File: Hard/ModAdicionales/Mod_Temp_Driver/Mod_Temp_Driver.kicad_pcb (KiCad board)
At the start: 2 copper layers, 70 x 100 mm, 0 parts

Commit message: Inicio placement de componentes en Modulos Adicionales
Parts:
- added C301: 1nF, Capacitor_SMD:C_0805_2012Metric_Pad1.15x1.40mm_HandSolder, F.Cu at (100.0, 137.0)
- added C302: 1nF, Capacitor_SMD:C_0805_2012Metric_Pad1.15x1.40mm_HandSolder, F.Cu at (107.5, 136.5)
- added C303: 1nF, Capacitor_SMD:C_0805_2012Metric_Pad1.15x1.40mm_HandSolder, F.Cu at (115.5, 138.0)
- added C304: 1nF, Capacitor_SMD:C_0805_2012Metric_Pad1.15x1.40mm_HandSolder, F.Cu at (104.0, 137.0)
- added C401: 100nF, Capacitor_SMD:C_0805_2012Metric_Pad1.15x1.40mm_HandSolder, F.Cu at (138.5, 135.0)
- added C402: 1nF, Capacitor_SMD:C_0805_2012Metric_Pad1.15x1.40mm_HandSolder, F.Cu at (138.5, 139.0)
- added C501: 2.2uf, Capacitor_THT:CP_Radial_D5.0mm_P2.00mm, F.Cu at (43.6, 76.8)
- added C502: 470nF x 400v, Capacitor_THT:C_Rect_L16.5mm_W8.7mm_P15.00mm_MKT, F.Cu at (4.65, 55.6)
- added D201: 1N4007, Diode_THT:D_DO-41_SOD81_P10.16mm_Horizontal, F.Cu at (81.0, 105.0)
- added D301: D_Zener 12v, Diode_THT:D_DO-35_SOD27_P7.62mm_Horizontal, F.Cu at (104.5, 125.0)
- added D401: 1N4148, Diode_THT:D_DO-35_SOD27_P7.62mm_Horizontal, F.Cu at (86.5, 130.5)
- added D402: 1N4148, Diode_THT:D_DO-35_SOD27_P7.62mm_Horizontal, F.Cu at (114.5, 117.0)
- added D403: 1N4148, Diode_THT:D_DO-35_SOD27_P7.62mm_Horizontal, F.Cu at (115.0, 102.5)
- added D501: 1N4148, Diode_THT:D_DO-35_SOD27_P7.62mm_Horizontal, F.Cu at (138.0, 72.5)
- added D502: 1N4007, Diode_THT:D_DO-41_SOD81_P10.16mm_Horizontal, F.Cu at (49.0, 50.6)
- added D503: 1N4148, Diode_SMD:D_MiniMELF, F.Cu at (90.0, 68.0)
- added H201: MountingHole, MountingHole:MountingHole_3.2mm_M3, F.Cu at (73.5, 52.5)
- added H202: MountingHole, MountingHole:MountingHole_3.2mm_M3, F.Cu at (73.5, 85.5)
- added H203: MountingHole, MountingHole:MountingHole_3.2mm_M3, F.Cu at (136.5, 52.5)
- added H204: MountingHole, MountingHole:MountingHole_3.2mm_M3, F.Cu at (136.5, 85.5)
- added H501: MountingHole, MountingHole:MountingHole_3.2mm_M3, F.Cu at (73.5, 92.5)
- added H502: MountingHole, MountingHole:MountingHole_3.2mm_M3, F.Cu at (73.5, 145.5)
- added H503: MountingHole, MountingHole:MountingHole_3.2mm_M3, F.Cu at (136.5, 92.5)
- added H504: MountingHole, MountingHole:MountingHole_3.2mm_M3, F.Cu at (136.5, 145.5)
- added J201: Conn_01x11_Female, Conectores:TerminalBlock_bornier-11_P5.00mm, F.Cu at (79.8, 93.0)
- added J202: Conn_02x05_Odd_Even, Connector_PinHeader_2.54mm:PinHeader_2x05_P2.54mm_Horizontal, F.Cu at (92.5, 142.5)
- added J203: Conn_02x10_Odd_Even, Connector_PinHeader_2.54mm:PinHeader_2x10_P2.54mm_Horizontal, F.Cu at (127.4, 142.5)
- added J501: Conn_02x10_Odd_Even, Connector_PinHeader_2.54mm:PinHeader_2x10_P2.54mm_Horizontal, F.Cu at (82.6, 55.5)
- added J502: Conn_02x05_Odd_Even, Connector_PinHeader_2.54mm:PinHeader_2x05_P2.54mm_Horizontal, F.Cu at (117.5, 55.5)
- added J503: Conn_01x06_Male, Conectores:TerminalBlock_bornier-6_P5.00mm, F.Cu at (117.5, 85.0)
- added K401: G5LE-1, Relay_THT:Relay_SPDT_Omron-G5LE-1, F.Cu at (92.0, 119.0)
- added K402: G5LE-1, Relay_THT:Relay_SPDT_Omron-G5LE-1, F.Cu at (119.5, 123.5)
- added K403: G5LE-1, Relay_THT:Relay_SPDT_Omron-G5LE-1, F.Cu at (119.5, 106.0)
- added K501: G5LE-1, Relay_THT:Relay_SPDT_Omron-G5LE-1, F.Cu at (132.5, 68.5)
- added Q401: BC857, Package_TO_SOT_SMD:SOT-23, F.Cu at (91.0, 131.5)
- added Q402: BC857, Package_TO_SOT_SMD:SOT-23, F.Cu at (125.5, 121.0)
- added Q403: BC857, Package_TO_SOT_SMD:SOT-23, F.Cu at (125.0, 103.5)
- added Q501: BC857, Package_TO_SOT_SMD:SOT-23, F.Cu at (99.0, 62.0)
- added R301: 220K, Resistor_SMD:R_0805_2012Metric_Pad1.15x1.40mm_HandSolder, F.Cu at (98.5, 125.0)
- added R302: 1ohm 1/4w, Resistor_THT:R_Axial_DIN0207_L6.3mm_D2.5mm_P7.62mm_Horizontal, F.Cu at (111.0, 111.0)
- added R303: 330K 1/4w (carbón), Resistor_THT:R_Axial_DIN0207_L6.3mm_D2.5mm_P7.62mm_Horizontal, F.Cu at (80.4, 109.0)
- added R304: 330K 1/4w (carbón), Resistor_THT:R_Axial_DIN0207_L6.3mm_D2.5mm_P7.62mm_Horizontal, F.Cu at (91.0, 109.0)
- added R305: 330K 1/4w (carbón), Resistor_THT:R_Axial_DIN0207_L6.3mm_D2.5mm_P7.62mm_Horizontal, F.Cu at (99.0, 112.0)
- added R306: 22K, Resistor_SMD:R_0805_2012Metric_Pad1.15x1.40mm_HandSolder, F.Cu at (98.5, 122.5)
- added R307: 1ohm 1/4w, Resistor_THT:R_Axial_DIN0207_L6.3mm_D2.5mm_P7.62mm_Horizontal, F.Cu at (111.0, 102.0)
- added R308: 1ohm 1/4w, Resistor_THT:R_Axial_DIN0207_L6.3mm_D2.5mm_P7.62mm_Horizontal, F.Cu at (111.0, 114.0)
- added R309: 1ohm 1/4w, Resistor_THT:R_Axial_DIN0207_L6.3mm_D2.5mm_P7.62mm_Horizontal, F.Cu at (111.0, 108.0)
- added R310: 220 1/4w, Resistor_THT:R_Axial_DIN0207_L6.3mm_D2.5mm_P7.62mm_Horizontal, F.Cu at (109.0, 125.0)
- added R311: 1ohm 1/4w, Resistor_THT:R_Axial_DIN0207_L6.3mm_D2.5mm_P7.62mm_Horizontal, F.Cu at (111.0, 105.0)
- added R312: 10k, Resistor_SMD:R_0805_2012Metric_Pad1.15x1.40mm_HandSolder, F.Cu at (97.5, 131.5)
- added R313: RA, Resistor_SMD:R_0805_2012Metric_Pad1.15x1.40mm_HandSolder, F.Cu at (109.5, 127.7)
- added R314: 1k, Resistor_SMD:R_0805_2012Metric_Pad1.15x1.40mm_HandSolder, F.Cu at (109.5, 129.5)
- added R315: 22k, Resistor_SMD:R_0805_2012Metric_Pad1.15x1.40mm_HandSolder, F.Cu at (113.5, 127.5)
- added R316: 150k, Resistor_SMD:R_0805_2012Metric_Pad1.15x1.40mm_HandSolder, F.Cu at (113.5, 129.5)
- added R317: 10k, Resistor_SMD:R_0805_2012Metric_Pad1.15x1.40mm_HandSolder, F.Cu at (115.5, 134.0)
- added R401: 10k, Resistor_SMD:R_0805_2012Metric_Pad1.15x1.40mm_HandSolder, F.Cu at (94.0, 129.5)
- added R402: 1M, Resistor_SMD:R_0805_2012Metric_Pad1.15x1.40mm_HandSolder, F.Cu at (91.0, 128.5)
- added R403: 10k, Resistor_SMD:R_0805_2012Metric_Pad1.15x1.40mm_HandSolder, F.Cu at (133.0, 140.0)
- added R404: 10k, Resistor_SMD:R_0805_2012Metric_Pad1.15x1.40mm_HandSolder, F.Cu at (125.5, 126.0)
- added R405: 10k, Resistor_SMD:R_0805_2012Metric_Pad1.15x1.40mm_HandSolder, F.Cu at (125.0, 108.5)
- added R406: 1M, Resistor_SMD:R_0805_2012Metric_Pad1.15x1.40mm_HandSolder, F.Cu at (125.5, 124.0)
- added R407: 1M, Resistor_SMD:R_0805_2012Metric_Pad1.15x1.40mm_HandSolder, F.Cu at (125.0, 106.5)
- added R408: 100k, Resistor_SMD:R_0805_2012Metric_Pad1.15x1.40mm_HandSolder, F.Cu at (129.5, 103.5)
- added R409: 100K, Resistor_SMD:R_0805_2012Metric_Pad1.15x1.40mm_HandSolder, F.Cu at (133.5, 123.5)
- added R410: 100k, Resistor_SMD:R_0805_2012Metric_Pad1.15x1.40mm_HandSolder, F.Cu at (135.5, 123.5)
- added R411: 100K, Resistor_SMD:R_0805_2012Metric_Pad1.15x1.40mm_HandSolder, F.Cu at (131.5, 103.5)
- added R412: 10k, Resistor_SMD:R_0805_2012Metric_Pad1.15x1.40mm_HandSolder, F.Cu at (130.5, 108.5)
- added R413: RA, Resistor_SMD:R_0805_2012Metric_Pad1.15x1.40mm_HandSolder, F.Cu at (130.5, 106.5)
- added R501: 10k, Resistor_SMD:R_0805_2012Metric_Pad1.15x1.40mm_HandSolder, F.Cu at (93.0, 60.0)
- added R502: 1M, Resistor_SMD:R_0805_2012Metric_Pad1.15x1.40mm_HandSolder, F.Cu at (95.5, 62.0)
- added R503: 10K, Resistor_SMD:R_0805_2012Metric_Pad1.15x1.40mm_HandSolder, F.Cu at (105.0, 68.5)
- added R504: 22K 1/4w (carbón), Resistor_THT:R_Axial_DIN0207_L6.3mm_D2.5mm_P7.62mm_Horizontal, F.Cu at (81.5, 73.0)
- added R505: 22K 1/4w (carbón), Resistor_THT:R_Axial_DIN0207_L6.3mm_D2.5mm_P7.62mm_Horizontal, F.Cu at (77.5, 80.5)
- added R506: 22K 1/4w (carbón), Resistor_THT:R_Axial_DIN0207_L6.3mm_D2.5mm_P7.62mm_Horizontal, F.Cu at (74.0, 73.0)
- added R507: 270 2w, Resistor_THT:R_Axial_DIN0516_L15.5mm_D5.0mm_P20.32mm_Horizontal, F.Cu at (2.30, 47.2)
- added REF**: SolderWirePad_1x01_Drill1.5mm, Connector_Wire:SolderWirePad_1x01_Drill1.5mm, F.Cu at (76.0, 100.0)
- added REF**: SolderWirePad_1x01_Drill1.5mm, Connector_Wire:SolderWirePad_1x01_Drill1.5mm, F.Cu at (81.5, 100.0)
- added REF**: SolderWirePad_1x01_Drill1.5mm, Connector_Wire:SolderWirePad_1x01_Drill1.5mm, F.Cu at (87.0, 100.0)
- added REF**: SolderWirePad_1x01_Drill1.5mm, Connector_Wire:SolderWirePad_1x01_Drill1.5mm, F.Cu at (91.0, 137.5)
- added REF**: SolderWirePad_1x01_Drill1.5mm, Connector_Wire:SolderWirePad_1x01_Drill1.5mm, F.Cu at (85.5, 137.5)
- added REF**: SolderWirePad_1x01_Drill1.5mm, Connector_Wire:SolderWirePad_1x01_Drill1.5mm, F.Cu at (80.0, 137.5)
- added U301: LM2904, Package_SO:SO-8_3.9x4.9mm_P1.27mm, F.Cu at (102.0, 130.9)
- added U302: LM2904, Package_SO:SO-8_3.9x4.9mm_P1.27mm, F.Cu at (111.5, 135.0)
- added U401: LM2904, Package_SO:SO-8_3.9x4.9mm_P1.27mm, F.Cu at (132.9, 136.1)
- added U501: PC817, Package_DIP:DIP-4_W7.62mm, F.Cu at (87.5, 80.5)
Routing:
- net /ProbadorDriver/(+)Load: track 0.00 -> 31.9 mm
- net GNDA: track 0.00 -> 26.3 mm
- net /ProbadorDriver/(-)Load: track 0.00 -> 25.7 mm
- net GND: track 0.00 -> 23.9 mm
- net +12V: track 0.00 -> 16.2 mm
- net Net-(D201-Pad2): track 0.00 -> 13.7 mm
- net /ProbadorDriver/(+)Driver_In: track 0.00 -> 9.33 mm
- net Net-(D401-Pad1): track 0.00 -> 8.12 mm
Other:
- board size 70 x 100 mm -> 70 x 102 mm
- net class 220 added: clearance 2, trace_width 3, via_dia 2.5, via_drill 1
- net class Default: clearance 0.2 -> 0.5; trace_width 0.25 -> 1; via_dia 0.8 -> 1.5; via_drill 0.4 -> 0.8
- rule trace_clearance: 0.2 -> 0.5

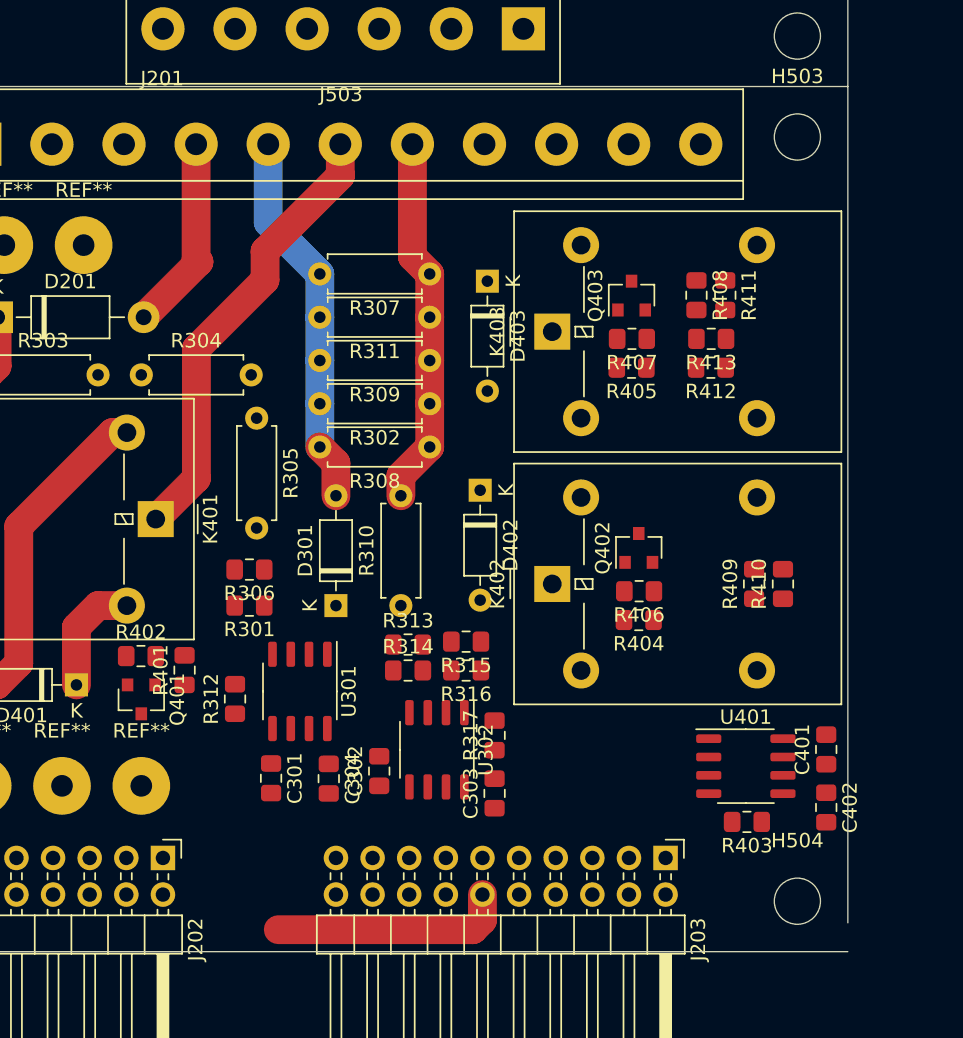
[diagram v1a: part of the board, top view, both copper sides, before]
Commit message: Avance en trazado de PCB modulos Adicionales
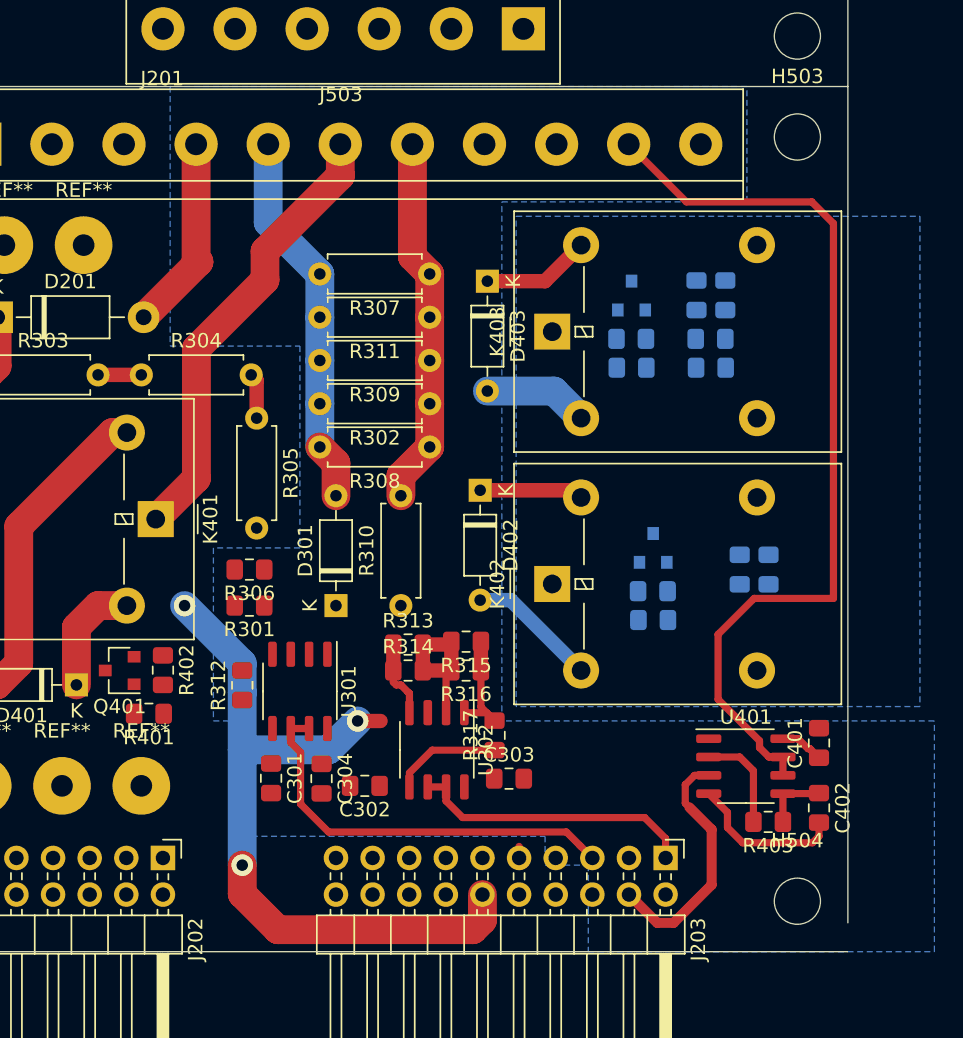
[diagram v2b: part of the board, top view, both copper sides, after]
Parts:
- Q402, Q403, R404, R405, R406, R407, R408, R409, R410, R411, R412, R413: moved to B.Cu
- moved R401 3.91 mm to (91.5, 132.5), turned to 180 degrees
- moved R410 3.16 mm to (132.5, 122.5)
- moved Q401 2.50 mm to (89.5, 129.5), turned to 180 degrees
- moved R408 2.00 mm to (131.5, 103.5)
- moved R411 2.00 mm to (129.5, 103.5)
- moved R402 1.81 mm to (92.5, 129.5), turned to 270 degrees
- moved R403 1.47 mm to (134.5, 140.0)
- moved C302 1.43 mm to (106.5, 137.5), turned to 180 degrees
- moved C303 1.43 mm to (116.5, 137.0), turned to 0 degrees
- moved R409 1.41 mm to (134.5, 122.5)
- moved R312 1.07 mm to (98.0, 130.5)
- moved Q402 1.00 mm to (126.5, 121.0)
- moved R404 1.00 mm to (126.5, 126.0), turned to 0 degrees
- moved R406 0.95 mm to (126.5, 124.0), turned to 0 degrees
- moved C401 0.67 mm to (138.0, 134.5)
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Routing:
- net /ProbadorDriver/(+)V_Dimmer: track 0.00 -> 63.7 mm
- net +12V: track 16.2 -> 54.9 mm, vias 0 -> 3
- net /ProbadorDriver/Out_Analog1: track 0.00 -> 28.6 mm
- net /ProbadorDriver/Out_Analog0: track 0.00 -> 19.9 mm
- net /ProbadorDriver/In_Analog0: track 0.00 -> 17.2 mm
- net GNDA: track 26.3 -> 42.7 mm
- net GND: track 23.9 -> 40.2 mm
- net Net-(R313-Pad2): track 0.00 -> 10.9 mm
- net Net-(R315-Pad1): track 0.00 -> 8.19 mm
- net Net-(D403-Pad1): track 0.00 -> 7.54 mm
- net Net-(C302-Pad1): track 0.00 -> 7.53 mm
- net Net-(D402-Pad1): track 0.00 -> 7.21 mm
- net Net-(R403-Pad2): track 0.00 -> 7.04 mm
- net Net-(C402-Pad1): track 0.00 -> 4.48 mm
- net Net-(R304-Pad2): track 0.00 -> 3.16 mm
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- added copper zone on B.Cu, net GND
- added copper zone on B.Cu, net GNDA

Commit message: Avance en trazado de pistas Modulos Adicionales
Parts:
- C301, C401: moved to B.Cu
- D401, D402, D403, D501: value 1N4148 -> 1N4007; footprint Diode_THT:D_DO-35_SOD27_P7.62mm_Horizontal -> Diode_THT:D_DO-41_SOD81_P10.16mm_Horizontal
- moved C502 79.4 mm to (81.0, 77.5), turned to 90 degrees
- moved R507 72.1 mm to (73.5, 58.5), turned to 270 degrees
- moved C501 55.8 mm to (97.5, 62.5), turned to 90 degrees
- moved D502 52.1 mm to (92.3, 79.5)
- moved D501 39.5 mm to (99.0, 66.5), turned to 180 degrees
- moved R505 22.8 mm to (98.5, 71.5), turned to 180 degrees
- moved R504 21.2 mm to (102.5, 76.0), turned to 180 degrees
- moved U501 16.8 mm to (102.5, 73.0)
- moved R506 13.6 mm to (87.5, 71.0)
- moved D503 13.6 mm to (102.0, 61.5)
- moved C302 12.5 mm to (118.5, 134.0), turned to 0 degrees
- moved K501 9.82 mm to (130.0, 78.0), turned to 180 degrees
- moved Q501 7.07 mm to (92.0, 63.0)
- moved R502 7.07 mm to (88.5, 63.0)
- moved R503 7.04 mm to (105.5, 61.5)
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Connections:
- K402 pad 3: /ProbadorDriver/(+)R_Dimmer -> Net-(K402-Pad3)
- K402 pad 4: Net-(K402-Pad4) -> /ProbadorDriver/(-)R_Dimmer
- K403 pad 1: /ProbadorDriver/(-)R_Dimmer -> /ProbadorDriver/(+)R_Dimmer
- R401 pad 1: /ProbadorDriver/In_Digital0 -> /ProbadorDriver/In_Digital2
- R405 pad 1: /ProbadorDriver/In_Digital2 -> /ProbadorDriver/In_Digital0
- R409 pad 1: /ProbadorDriver/(+)R_Dimmer -> Net-(K402-Pad3)
- R409 pad 2: Net-(K402-Pad4) -> /ProbadorDriver/(-)R_Dimmer
- R410 pad 1: /ProbadorDriver/(+)R_Dimmer -> Net-(K402-Pad3)
- R410 pad 2: Net-(K402-Pad4) -> /ProbadorDriver/(-)R_Dimmer
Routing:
- net +12V: track 54.9 -> 171.4 mm, vias 3 -> 8
- net /ProbadorTemporizador/In_N_220: track 0.00 -> 91.3 mm
- net /ProbadorDriver/In_Digital0: track 0.80 -> 53.4 mm, vias 0 -> 2
- net +12VA: track 0.00 -> 51.1 mm, vias 0 -> 2
- net /ProbadorDriver/(-)R_Dimmer: track 0.00 -> 50.1 mm
- net GNDS: track 0.00 -> 43.8 mm, vias 0 -> 1
- net Net-(D501-Pad1): track 0.00 -> 37.6 mm
- net /ProbadorTemporizador/Fase: track 0.00 -> 36.2 mm
- net GNDA: track 42.7 -> 77.0 mm, vias 0 -> 5
- net /ProbadorDriver/In_Digital2: track 0.00 -> 29.9 mm, vias 0 -> 2
- net Net-(K402-Pad1): track 0.00 -> 26.7 mm, vias 0 -> 1
- net /ProbadorDriver/In_Digital1: track 0.00 -> 23.5 mm, vias 0 -> 2
- net Net-(D301-Pad1): track 0.00 -> 18.7 mm
- net /ProbadorTemporizador/Disparo: track 0.00 -> 17.4 mm
- net GNDPWR: track 0.00 -> 17.1 mm
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- added copper zone on B.Cu, net GNDS
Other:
- board size 70 x 102 mm -> 70 x 100 mm

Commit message: Primera version de PCBs para fabricar
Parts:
- moved D502 13.8 mm to (105.8, 76.5)
- moved R504 0.71 mm to (102.0, 76.5)
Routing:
- net /ProbadorTemporizador/In_N_220: track 91.3 -> 133.5 mm
- net /ProbadorTemporizador/Carga: track 0.00 -> 26.1 mm
- net Net-(C502-Pad2): track 0.00 -> 10.3 mm
- net Net-(D502-Pad1): track 0.00 -> 7.55 mm
- net Net-(R504-Pad2): track 0.00 -> 7.21 mm
- net Net-(R505-Pad2): track 0.00 -> 3.59 mm
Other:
- outline, holes or cut-outs redrawn
- rule trace_min: 0.2 -> 0.5
- rule via_min_size: 0.4 -> 0.7
- board text added: "CESE-FIUBA Test Drivers"
- board text added: "CESE-FIUBA Test Temporizador"
- board text added: "Gonzalo Gontad"
